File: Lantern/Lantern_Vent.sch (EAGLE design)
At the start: 9 parts

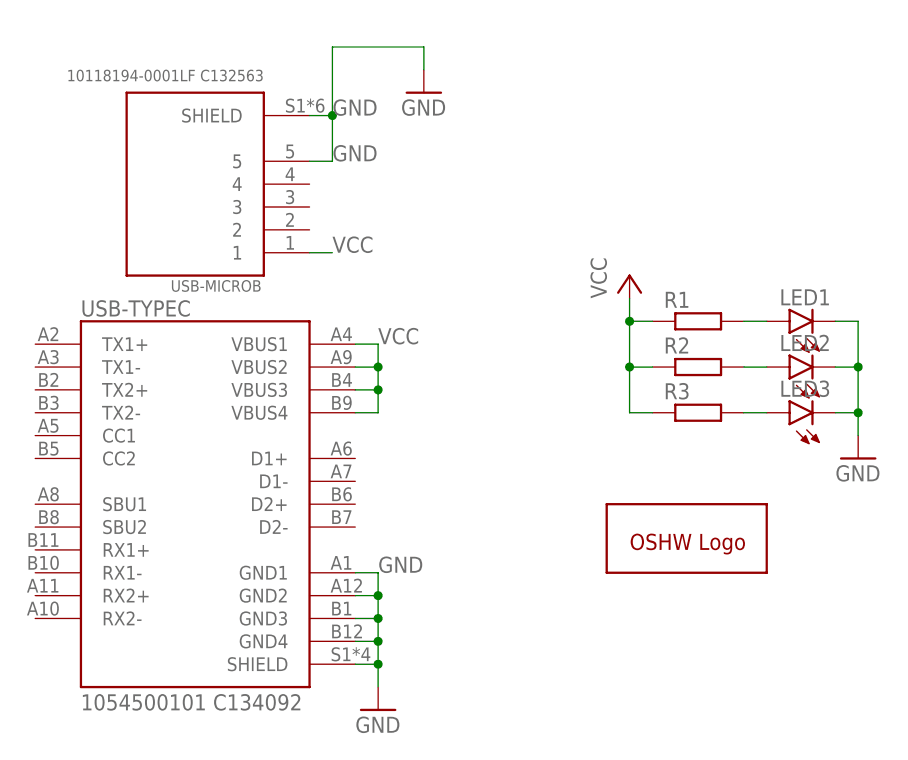
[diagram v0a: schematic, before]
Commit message: Added Fuse
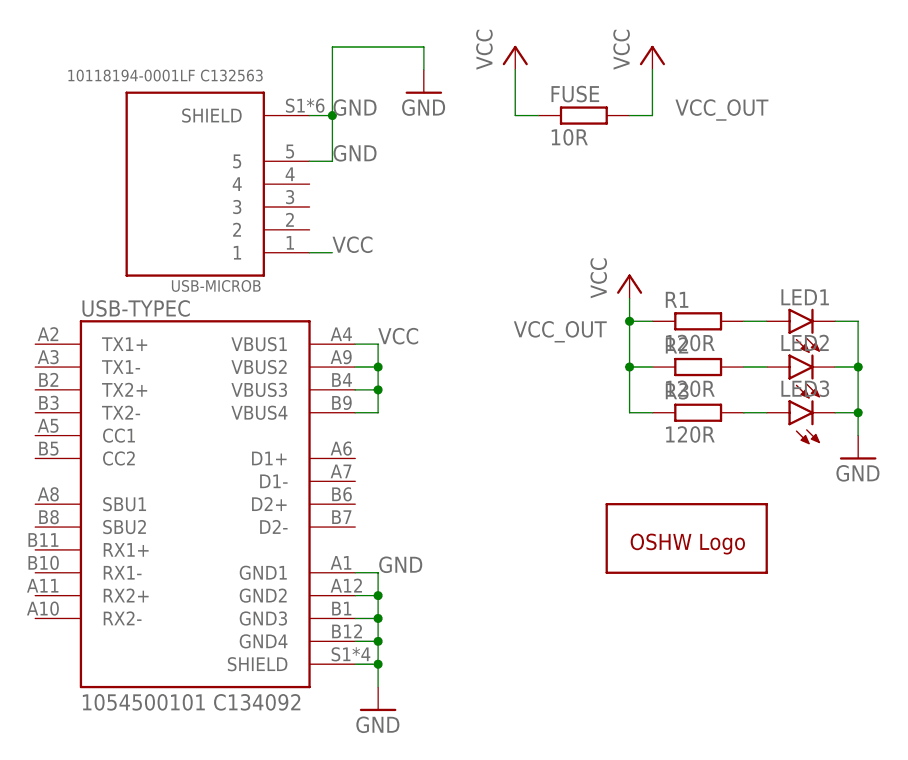
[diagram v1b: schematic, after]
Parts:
- added FUSE: 10R, rcl:R-EU_R0805
- R1, R2, R3: value (none) -> 120R
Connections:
- new net VCC_OUT: FUSE.2, R1.1, R2.1, R3.1
- net VCC: now also FUSE.1; no longer R1.1, R2.1, R3.1
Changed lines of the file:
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@@
 <part name="GND5" library="supply1" library_urn="urn:adsk.eagle:library:371" deviceset="GND" device=""/>
 <part name="GND6" library="supply1" library_urn="urn:adsk.eagle:library:371" deviceset="GND" device=""/>
-<part name="R1" library="rcl" library_urn="urn:adsk.eagle:library:334" deviceset="R-EU_" device="R0805" package3d_urn="urn:adsk.eagle:package:23553/2"/>
-<part name="R2" library="rcl" library_urn="urn:adsk.eagle:library:334" deviceset="R-EU_" device="R0805" package3d_urn="urn:adsk.eagle:package:23553/2"/>
-<part name="R3" library="rcl" library_urn="urn:adsk.eagle:library:334" deviceset="R-EU_" device="R0805" package3d_urn="urn:adsk.eagle:package:23553/2"/>
+<part name="R1" library="rcl" library_urn="urn:adsk.eagle:library:334" deviceset="R-EU_" device="R0805" package3d_urn="urn:adsk.eagle:package:23553/2" value="120R"/>
+<part name="R2" library="rcl" library_urn="urn:adsk.eagle:library:334" deviceset="R-EU_" device="R0805" package3d_urn="urn:adsk.eagle:package:23553/2" value="120R"/>
+<part name="R3" library="rcl" library_urn="urn:adsk.eagle:library:334" deviceset="R-EU_" device="R0805" package3d_urn="urn:adsk.eagle:package:23553/2" value="120R"/>
 <part name="LED1" library="led" library_urn="urn:adsk.eagle:library:259" deviceset="LED" device="CHIP-LED0805" package3d_urn="urn:adsk.eagle:package:15818/2"/>
 <part name="LED2" library="led" library_urn="urn:adsk.eagle:library:259" deviceset="LED" device="CHIP-LED0805" package3d_urn="urn:adsk.eagle:package:15818/2"/>
@@
 <part name="P+1" library="supply1" library_urn="urn:adsk.eagle:library:371" deviceset="VCC" device=""/>
 <part name="GOLD_ORB_SM1" library="oshw" deviceset="OSHWLOGO" device="LOGO5MM"/>
+<part name="FUSE" library="rcl" library_urn="urn:adsk.eagle:library:334" deviceset="R-EU_" device="R0805" package3d_urn="urn:adsk.eagle:package:23553/2" value="10R"/>
+<part name="P+2" library="supply1" library_urn="urn:adsk.eagle:library:371" deviceset="VCC" device=""/>
+<part name="P+3" library="supply1" library_urn="urn:adsk.eagle:library:371" deviceset="VCC" device=""/>
 </parts>
 <sheets>
@@
 </instance>
 <instance part="GOLD_ORB_SM1" gate="G$1" x="66.04" y="22.86" smashed="yes"/>
+<instance part="FUSE" gate="G$1" x="63.5" y="73.66" smashed="yes">
+<attribute name="NAME" x="59.69" y="75.1586" size="1.778" layer="95"/>
+<attribute name="VALUE" x="59.69" y="70.358" size="1.778" layer="96"/>
+</instance>
+<instance part="P+2" gate="VCC" x="71.12" y="81.28" smashed="yes">
+<attribute name="VALUE" x="68.58" y="78.74" size="1.778" layer="96" rot="R90"/>
+</instance>
+<instance part="P+3" gate="VCC" x="55.88" y="81.28" smashed="yes">
+<attribute name="VALUE" x="53.34" y="78.74" size="1.778" layer="96" rot="R90"/>
+</instance>
 </instances>
 <busses>
@@
 </segment>
 <segment>
+<pinref part="P+3" gate="VCC" pin="VCC"/>
+<wire x1="55.88" y1="78.74" x2="55.88" y2="73.66" width="0.1524" layer="91"/>
+<pinref part="FUSE" gate="G$1" pin="1"/>
+<wire x1="55.88" y1="73.66" x2="58.42" y2="73.66" width="0.1524" layer="91"/>
+</segment>
+</net>
+<net name="N$1" class="0">
+<segment>
+<pinref part="R1" gate="G$1" pin="2"/>
+<pinref part="LED1" gate="G$1" pin="A"/>
+<wire x1="83.82" y1="50.8" x2="81.28" y2="50.8" width="0.1524" layer="91"/>
+</segment>
+</net>
+<net name="N$2" class="0">
+<segment>
+<pinref part="R2" gate="G$1" pin="2"/>
+<pinref part="LED2" gate="G$1" pin="A"/>
+<wire x1="83.82" y1="45.72" x2="81.28" y2="45.72" width="0.1524" layer="91"/>
+</segment>
+</net>
+<net name="N$3" class="0">
+<segment>
+<pinref part="R3" gate="G$1" pin="2"/>
+<pinref part="LED3" gate="G$1" pin="A"/>
+<wire x1="83.82" y1="40.64" x2="81.28" y2="40.64" width="0.1524" layer="91"/>
+</segment>
+</net>
+<net name="VCC_OUT" class="0">
+<segment>
+<pinref part="FUSE" gate="G$1" pin="2"/>
+<pinref part="P+2" gate="VCC" pin="VCC"/>
+<wire x1="68.58" y1="73.66" x2="71.12" y2="73.66" width="0.1524" layer="91"/>
+<wire x1="71.12" y1="73.66" x2="71.12" y2="78.74" width="0.1524" layer="91"/>
+<label x="73.66" y="73.66" size="1.778" layer="95"/>
+</segment>
+<segment>
 <pinref part="R1" gate="G$1" pin="1"/>
 <wire x1="71.12" y1="50.8" x2="68.58" y2="50.8" width="0.1524" layer="91"/>
@@
 <wire x1="68.58" y1="50.8" x2="68.58" y2="53.34" width="0.1524" layer="91"/>
 <junction x="68.58" y="50.8"/>
-</segment>
-</net>
-<net name="N$1" class="0">
-<segment>
-<pinref part="R1" gate="G$1" pin="2"/>
-<pinref part="LED1" gate="G$1" pin="A"/>
-<wire x1="83.82" y1="50.8" x2="81.28" y2="50.8" width="0.1524" layer="91"/>
-</segment>
-</net>
-<net name="N$2" class="0">
-<segment>
-<pinref part="R2" gate="G$1" pin="2"/>
-<pinref part="LED2" gate="G$1" pin="A"/>
-<wire x1="83.82" y1="45.72" x2="81.28" y2="45.72" width="0.1524" layer="91"/>
-</segment>
-</net>
-<net name="N$3" class="0">
-<segment>
-<pinref part="R3" gate="G$1" pin="2"/>
-<pinref part="LED3" gate="G$1" pin="A"/>
-<wire x1="83.82" y1="40.64" x2="81.28" y2="40.64" width="0.1524" layer="91"/>
-</segment>
-</net>
+<label x="66.04" y="50.8" size="1.778" layer="95" rot="R180"/>
+</segment>
+</net>
